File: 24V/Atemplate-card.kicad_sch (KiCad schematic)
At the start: 3 parts, among them J1 Conn_01x10_Pin, SW1 SW_DPDT_x2

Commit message: pushing again
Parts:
- removed SW1: SW_DPDT_x2, 2024-backplane:SW_CUI_DPDT, symbol Switch:SW_DPDT_x2
- added C1: 100uF/100v, symbol Device:C_Polarized
- added C2: 470uF/50v, symbol Device:C_Polarized
- added PS1: VCF4824EBO-75WFR3-N, 2024-power:Mornsun VCF4824EBO-75WFR3-N, symbol 2024-power:Mornsun_VCF4824EBO-75WFR3-N
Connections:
- net 24v: now also C2.1, PS1.7 (+Sense), PS1.8 (+Vo)
- net 48v: now also C1.1, PS1.1 (+Vin)
- net GND2: now also C1.2, C2.2, PS1.2 (Ctrl), PS1.3 (-Vin), PS1.4 (0V), PS1.5 (-Sense)
- removed net 12v: J2.4 (12V), J2.5 (12V), J2.6 (12V)
- net rx0/scl0: no longer names the net of J1.3 (RX0/SCL0)
- net rx1/scl1: no longer names the net of J1.6 (RX1/SCL1)
- net rx2/scl2: no longer names the net of J1.9 (RX2/SCL2)
- net tx0/sda0: no longer names the net of J1.2 (TX0/SDA0)
- net tx1/sda1: no longer names the net of J1.5 (TX1/SDA1)
- net tx2/sda2: no longer names the net of J1.8 (TX2/SDA2)
- no-connect marks 0 -> 10

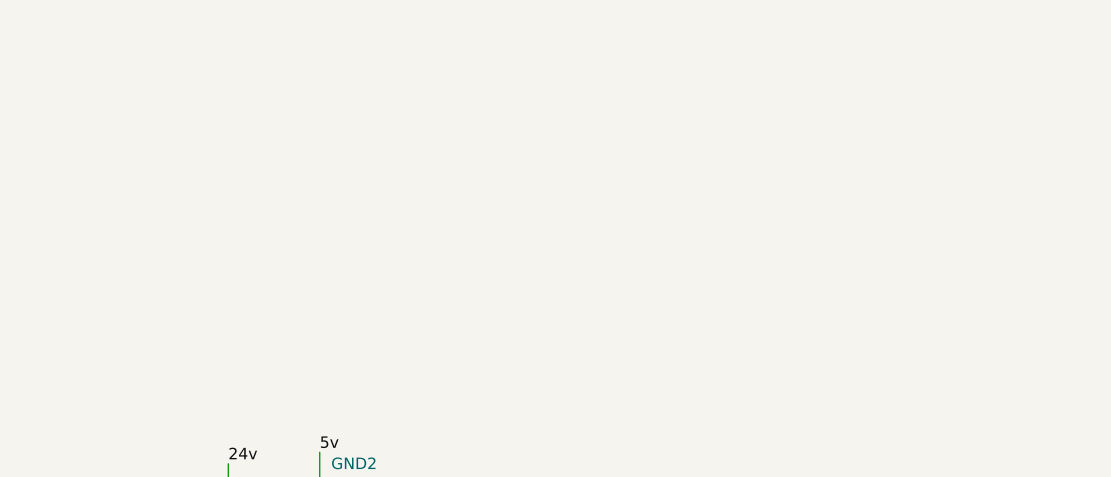
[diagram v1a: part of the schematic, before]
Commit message: Designed the 5v voltage regulator
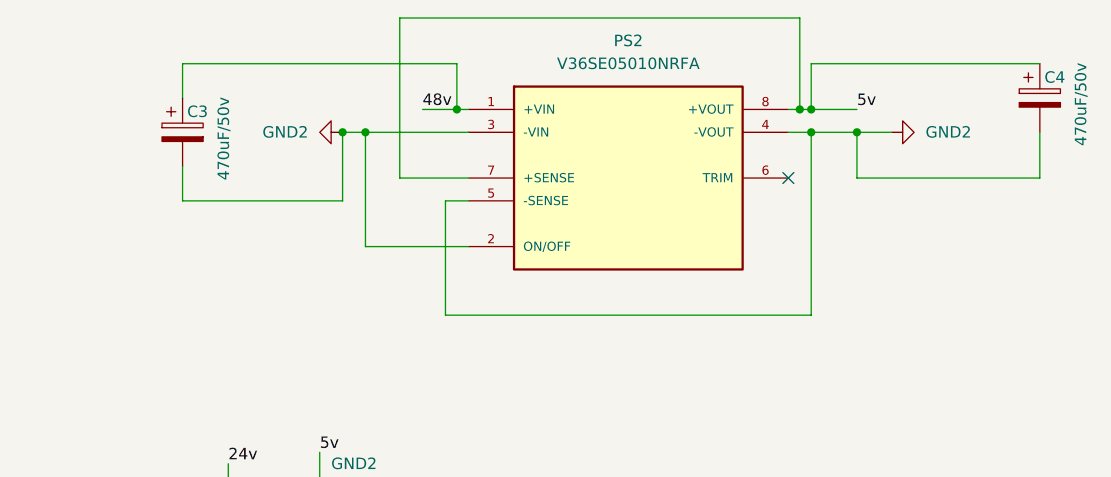
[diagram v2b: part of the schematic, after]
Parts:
- added C3, C4: 470uF/50v, Capacitor_SMD:CP_Elec_16x17.5, symbol Device:C_Polarized
- added PS2: V36SE05010NRFA, 2024-power:Delta V36SE05010NRFA, symbol 2024-power:Delta_V36SE05010NRFA
- C1, C2: footprint (none) -> Capacitor_SMD:CP_Elec_16x17.5
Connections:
- net 48v: now also C3.1, PS2.1 (+VIN)
- net 5v: now also C4.1, PS2.7 (+SENSE), PS2.8 (+VOUT)
- net GND2: now also C3.2, C4.2, PS2.2 (ON/OFF), PS2.3 (-VIN), PS2.4 (-VOUT), PS2.5 (-SENSE)
- no-connect marks 10 -> 11

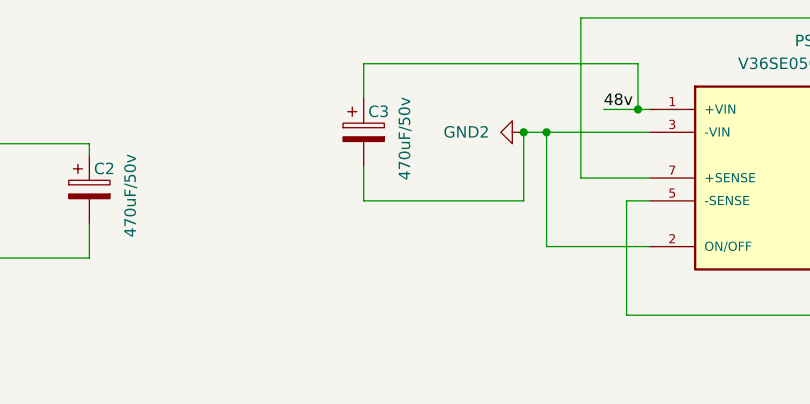
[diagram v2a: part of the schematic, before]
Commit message: Complete Power Boards
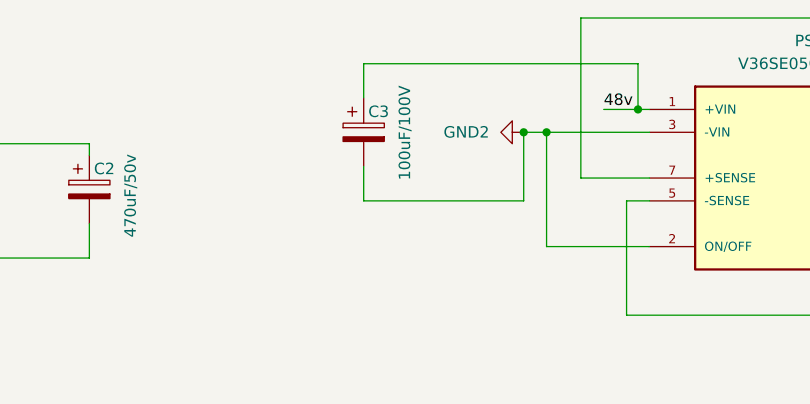
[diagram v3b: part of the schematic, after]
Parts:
- C1, C2, C4: footprint Capacitor_SMD:CP_Elec_16x17.5 -> Capacitor_SMD:CP_Elec_10x12.5
- C3: value 470uF/50v -> 100uF/100V; footprint Capacitor_SMD:CP_Elec_16x17.5 -> Capacitor_SMD:CP_Elec_10x12.5
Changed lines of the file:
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@@
 			)
 		)
-		(property "Footprint" "Capacitor_SMD:CP_Elec_16x17.5"
+		(property "Footprint" "Capacitor_SMD:CP_Elec_10x12.5"
 			(at 116.5352 88.9 0)
 			(effects
@@
 			)
 		)
-		(property "Value" "470uF/50v"
+		(property "Value" "100uF/100V"
 			(at 150.622 84.074 90)
 			(effects
@@
 			)
 		)
-		(property "Footprint" "Capacitor_SMD:CP_Elec_16x17.5"
+		(property "Footprint" "Capacitor_SMD:CP_Elec_10x12.5"
 			(at 147.0152 82.55 0)
 			(effects
@@
 			)
 		)
-		(property "Footprint" "Capacitor_SMD:CP_Elec_16x17.5"
+		(property "Footprint" "Capacitor_SMD:CP_Elec_10x12.5"
 			(at 31.4452 88.9 0)
 			(effects
@@
 			)
 		)
-		(property "Footprint" "Capacitor_SMD:CP_Elec_16x17.5"
+		(property "Footprint" "Capacitor_SMD:CP_Elec_10x12.5"
 			(at 242.2652 78.74 0)
 			(effects
